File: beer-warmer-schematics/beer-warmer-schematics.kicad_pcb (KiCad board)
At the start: 4 copper layers, 60 x 42.8 mm, 33 parts, among them J1 USB_C_Receptacle_USB2.0_14P, J2 Screw_Terminal_01x02, J3 Conn_01x07_Socket, J4 Conn_01x07_Socket, J5 Conn_01x04_Pin, J6 Screw_Terminal_01x03, Q1 AOD4184A, U2 LM2596S-5, U3 CH224K

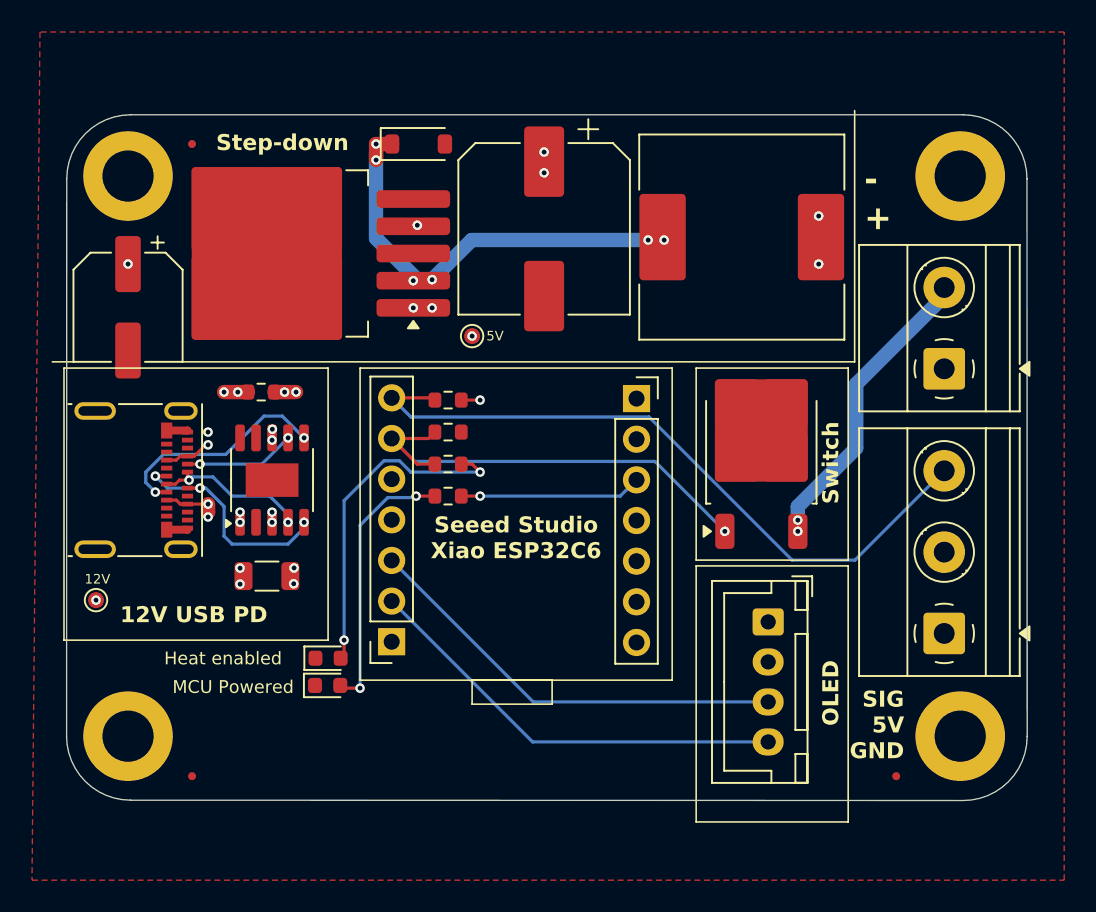
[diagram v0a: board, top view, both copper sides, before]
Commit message: fix a bunch of potential issues, add current sense
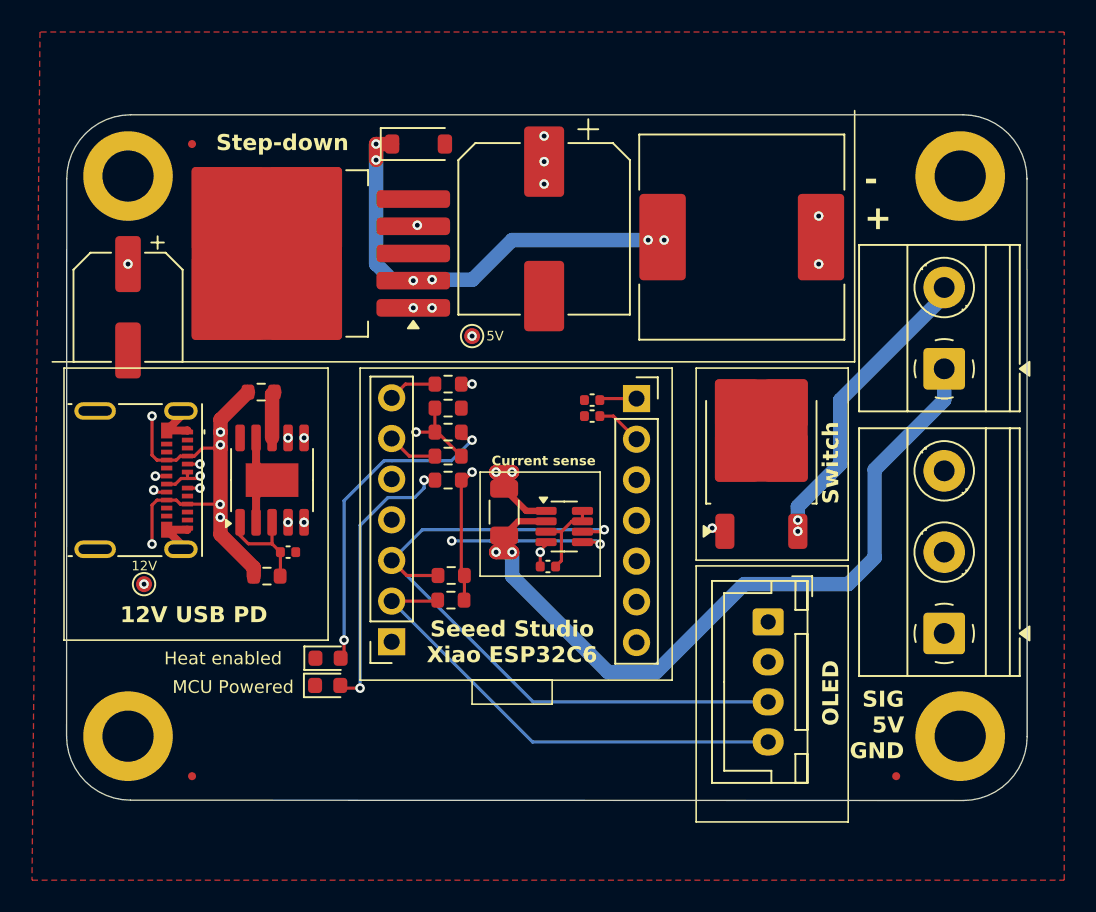
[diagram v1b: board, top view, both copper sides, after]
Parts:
- added C1: 1uF, Capacitor_SMD:C_0402_1005Metric, F.Cu at (152.5, 89.0)
- added C4: 1uF, Capacitor_SMD:C_0402_1005Metric, F.Cu at (152.5, 90.0)
- added C5: 1uF, Capacitor_SMD:C_0402_1005Metric, F.Cu at (149.7, 99.4)
- added C6: 1uF, Capacitor_SMD:C_0402_1005Metric, F.Cu at (133.5, 98.5)
- added R10: 2m, Resistor_SMD:R_1206_3216Metric, F.Cu at (147.0, 96.0)
- added R7: 200R, Resistor_SMD:R_0603_1608Metric, F.Cu at (143.5, 92.5)
- added R8: 4.7k, Resistor_SMD:R_0603_1608Metric, F.Cu at (143.7, 101.5)
- added R9: 4.7k, Resistor_SMD:R_0603_1608Metric, F.Cu at (143.7, 100.0)
- added U4: INA219AxDCN, Package_TO_SOT_SMD:SOT-23-8, F.Cu at (150.8, 96.9)
- R1: footprint Resistor_SMD:R_1206_3216Metric -> Resistor_SMD:R_0603_1608Metric
- moved TP1 3.16 mm to (124.5, 100.5)
- moved R3 2.00 mm to (143.5, 91.0)
- moved R2 1.50 mm to (143.5, 89.5)
- moved R4 1.00 mm to (143.5, 88.0)
- moved R6 1.00 mm to (143.5, 94.0)
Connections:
- net D3 renamed +3V3
- net Net-(J2-Pin_2) renamed HEAT-
- C2 pad 1: VDD -> VBUS
- J1 pad A4: Net-(J1-VBUS-PadA4) -> VBUS
- J1 pad A9: Net-(J1-VBUS-PadA4) -> VBUS
- J1 pad B4: Net-(J1-VBUS-PadA4) -> VBUS
- J1 pad B9: Net-(J1-VBUS-PadA4) -> VBUS
- J2 pad 1: VDD -> HEAT+
- J3 pad 2: GND -> Net-(J3-Pin_2)
- Q1 pad 1: D1 -> Net-(Q1-G)
- R1 pad 1: Net-(J1-VBUS-PadA4) -> VBUS
- R2 pad 1: D1 -> Net-(Q1-G)
- R3 pad 1: D1 -> Net-(Q1-G)
- R5 pad 1: Net-(J1-VBUS-PadA4) -> VBUS
- TP1 pad 1: VDD -> VBUS
- U2 pad 1: VDD -> VBUS
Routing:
- net HEAT+: track 0.00 -> 50.1 mm, vias 0 -> 2
- net VBUS: track 0.00 -> 33.4 mm, vias 0 -> 14
- net Net-(Q1-G): track 0.00 -> 26.9 mm, vias 0 -> 2
- net D1: track 29.4 -> 3.16 mm, vias 1 -> 0
- net Net-(J1-VBUS-PadA4): track 22.4 -> 0.00 mm, vias 8 -> 0
- net SDA: track 26.7 -> 45.5 mm, vias 0 -> 1
- net SCL: track 26.7 -> 45.4 mm, vias 0 -> 2
- net GND: track 2.78 -> 17.4 mm
- net +3V3: track 11.4 -> 20.8 mm
- net VDD: track 0.00 -> 6.62 mm, vias 11 -> 0
- net D0: track 43.8 -> 39.8 mm
- net +5V: track 1.18 -> 4.68 mm, vias 6 -> 7
- net Net-(J3-Pin_2): track 0.00 -> 2.89 mm
- net Net-(U3-VBUS): track 5.26 -> 2.92 mm, vias 4 -> 0
- net Net-(U3-DM): track 14.4 -> 12.5 mm
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- added copper zone on In2.Cu, net VBUS
- removed copper zone on In2.Cu, net VDD
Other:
- board text added: "Current sense"

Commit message: middle ground plane, 12v over dedicated tracks to avoid noise
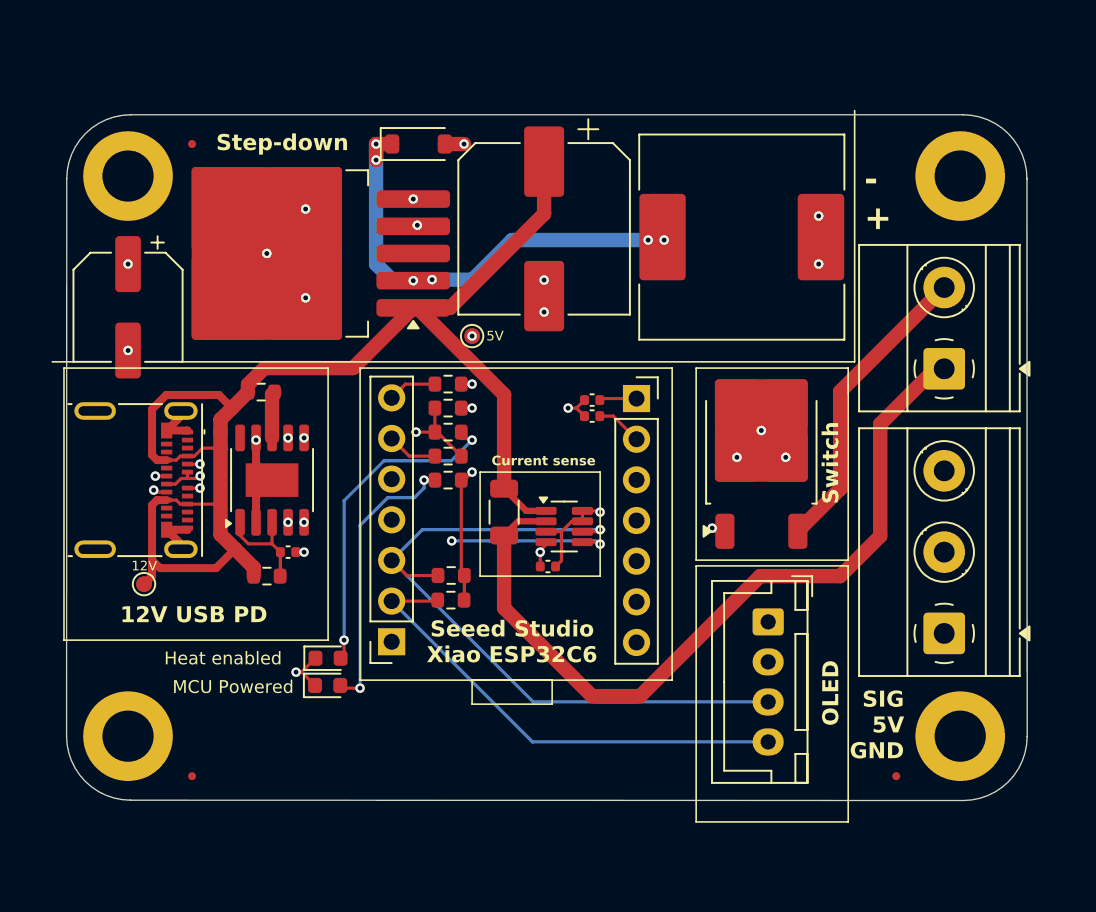
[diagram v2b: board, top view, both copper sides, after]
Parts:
- R10: value 2m -> 20m
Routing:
- net VBUS: track 33.4 -> 86.2 mm, vias 14 -> 0
- net GND: track 17.4 -> 26.0 mm, vias 0 -> 17
- net HEAT-: track 18.5 -> 19.0 mm, vias 2 -> 0
- net HEAT+: track 50.1 -> 49.9 mm, vias 2 -> 0
- added copper zone on In2.Cu, net GND
- removed copper zone on F.Cu, net GND
- removed copper zone on In2.Cu, net VBUS

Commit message: use a much simpler usb c component
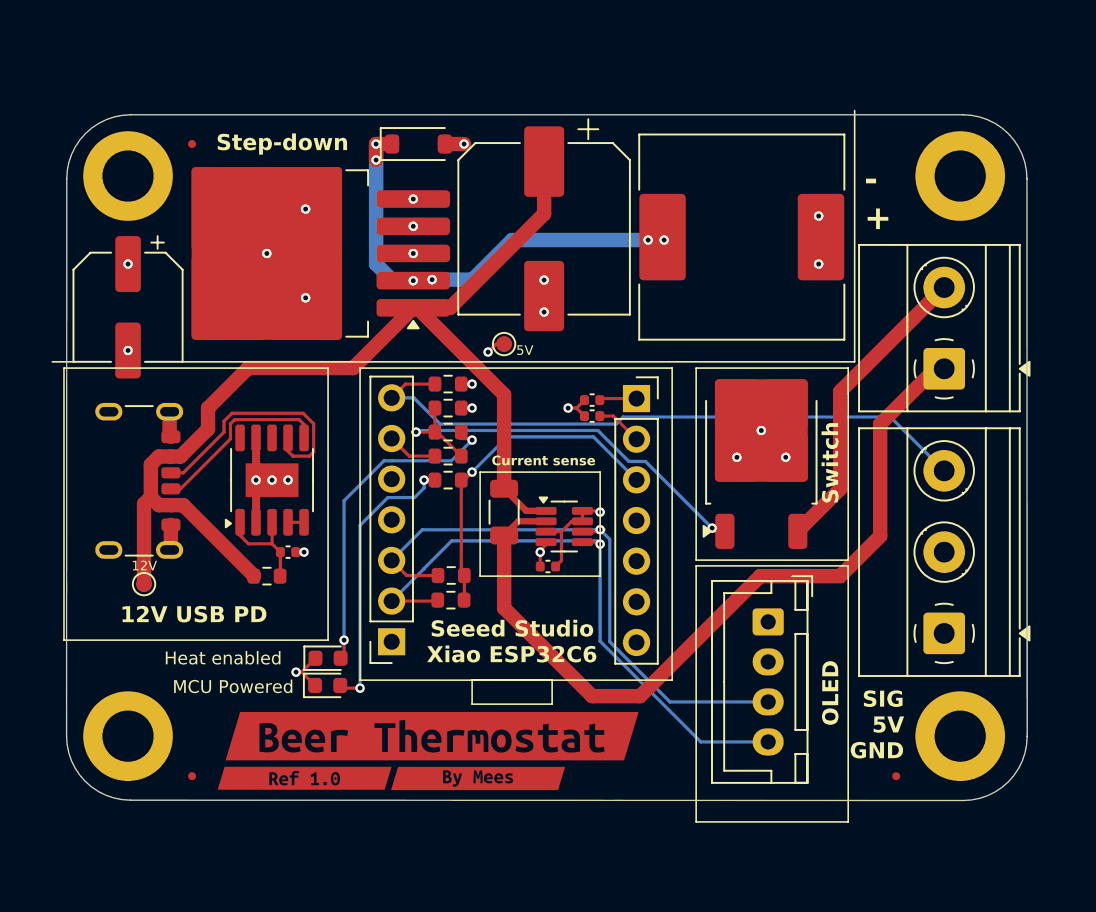
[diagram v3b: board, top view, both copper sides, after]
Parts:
- removed R5: 10K, Resistor_SMD:R_0603_1608Metric
- removed kibuzzard-67EA8950: G***, kibuzzard-67EA8950
- removed kibuzzard-67EA89B2: G***, kibuzzard-67EA89B2
- removed kibuzzard-67EA89F2: G***, kibuzzard-67EA89F2
- added kibuzzard-67EFB7C2: G***, kibuzzard-67EFB7C2, F.Cu at (142.5, 110.0)
- added kibuzzard-67EFB7CE: G***, kibuzzard-67EFB7CE, F.Cu at (134.5, 112.6)
- added kibuzzard-67EFB7D4: G***, kibuzzard-67EFB7D4, F.Cu at (145.4, 112.6)
- J1: footprint Library:USB_C_Receptacle_Molex_105450-0101 -> Connector_USB:USB_C_Receptacle_GCT_USB4125-xx-x_6P_TopMnt_Horizontal
- moved TP2 2.06 mm to (147.0, 85.5)
- moved J1 0.90 mm to (123.1, 94.0)
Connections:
- U3 pad 4: Net-(U3-DP) -> Net-(U3-DM)
- U3 pad 8: Net-(U3-VBUS) -> unconnected-(U3-VBUS-Pad8)
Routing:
- net VBUS: track 86.2 -> 68.8 mm
- net Net-(U3-DM): track 12.5 -> 1.00 mm, vias 3 -> 0
- net Net-(U3-DP): track 9.39 -> 0.00 mm, vias 2 -> 0
- net Net-(J1-CC1): track 6.96 -> 15.6 mm, vias 2 -> 0
- net SDA: track 45.5 -> 37.5 mm
- net SCL: track 45.4 -> 37.9 mm, vias 2 -> 1
- net Net-(U3-VBUS): track 2.92 -> 0.00 mm
- net GND: track 26.0 -> 23.4 mm, vias 17 -> 20
- net Net-(J1-CC2): track 13.6 -> 11.6 mm, vias 2 -> 0
- net +5V: track 4.68 -> 5.89 mm

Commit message: wider traces
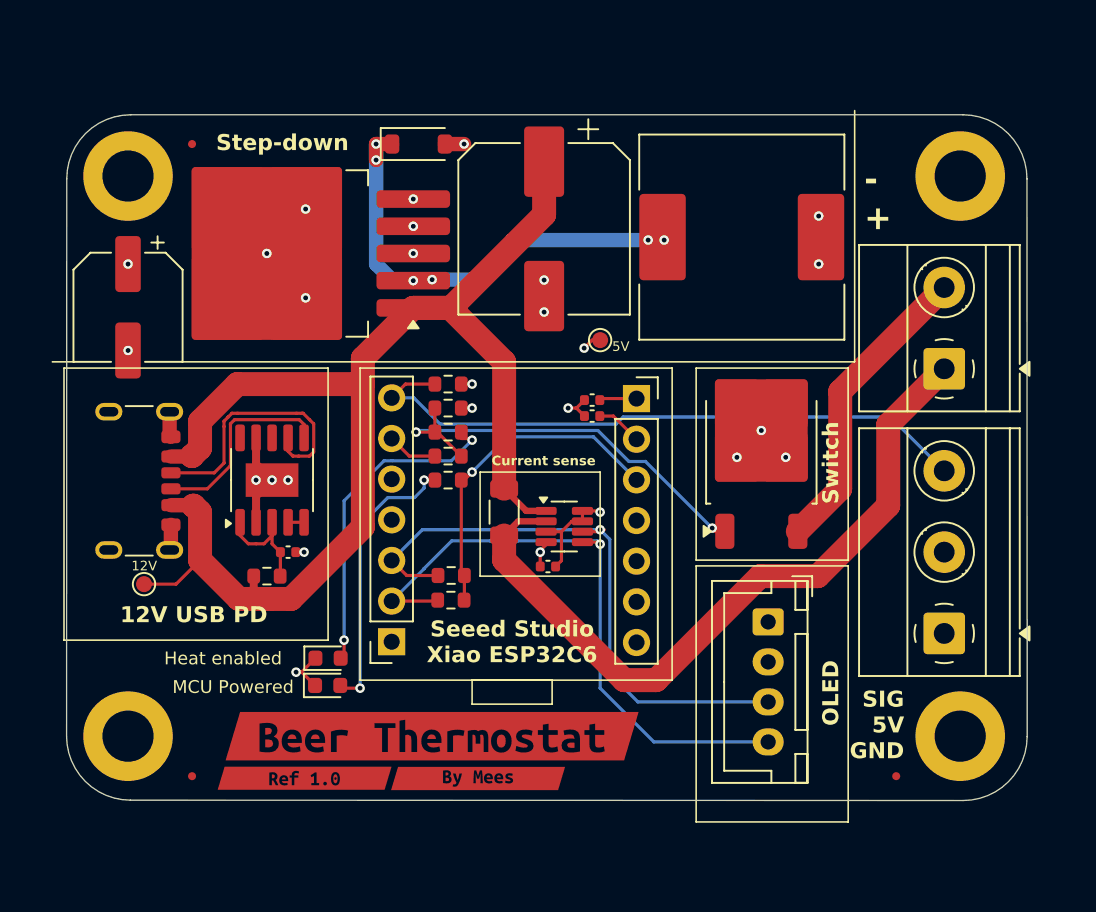
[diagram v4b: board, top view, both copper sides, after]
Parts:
- moved TP2 6.01 mm to (153.0, 85.3)
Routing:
- net VBUS: track 68.8 -> 86.1 mm
- net HEAT+: track 49.9 -> 46.2 mm
- net SCL: track 37.9 -> 39.7 mm
- net SDA: track 37.5 -> 38.7 mm
- net Net-(J1-CC1): track 15.6 -> 16.7 mm
- net VDD: track 6.62 -> 7.67 mm
- net Net-(J1-CC2): track 11.6 -> 12.6 mm

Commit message: clean up schematics, correct mosfet orientation
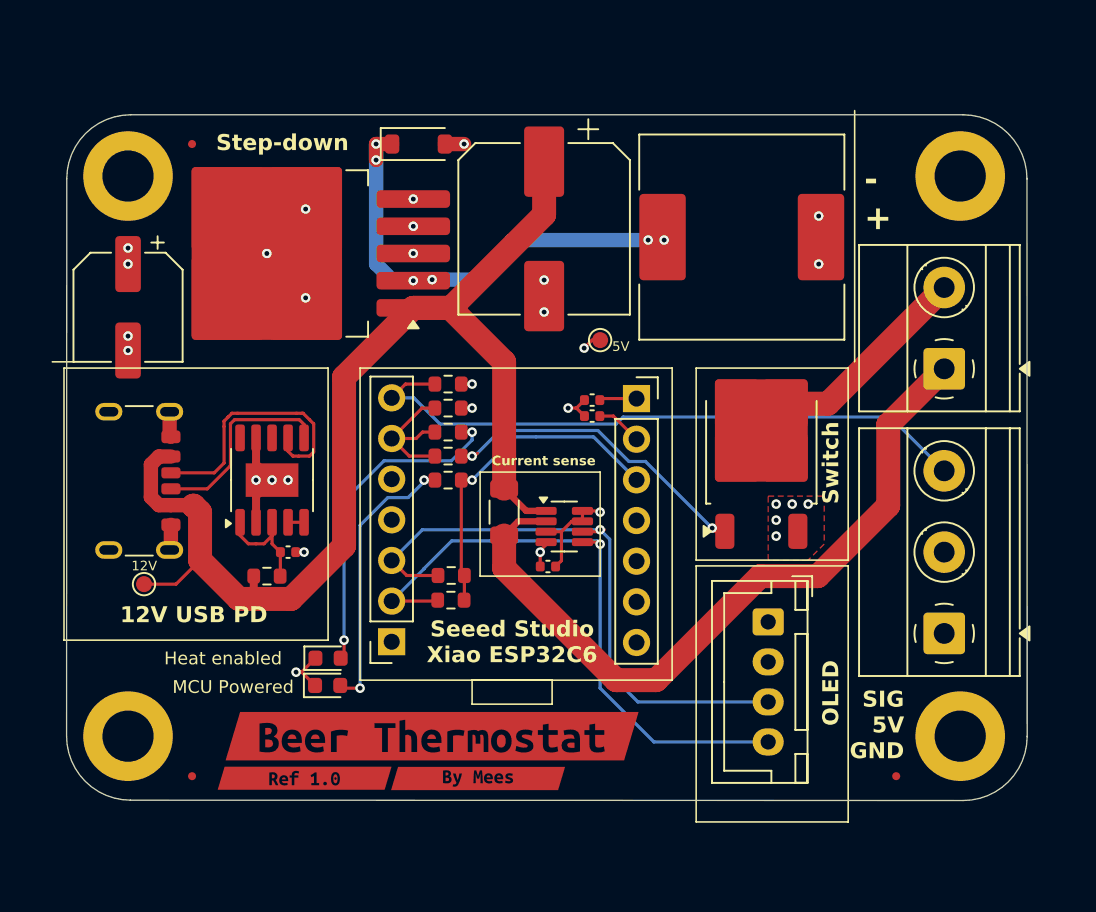
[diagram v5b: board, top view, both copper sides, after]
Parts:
- moved R8 1.54 mm to (143.7, 100.0), turned to 0 degrees
- moved R9 1.54 mm to (143.7, 101.5), turned to 0 degrees
- turned C1 to 180 degrees
- turned C5 to 180 degrees
- turned R7 to 0 degrees
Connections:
- C1 pad 1: GND -> +5V
- C1 pad 2: +5V -> GND
- C5 pad 1: +5V -> GND
- C5 pad 2: GND -> +5V
- Q1 pad 2: GND -> HEAT-
- Q1 pad 3: HEAT- -> GND
- R2 pad 1: Net-(Q1-G) -> D1
- R3 pad 1: Net-(Q1-G) -> D1
- R7 pad 1: Net-(Q1-G) -> D1
- R7 pad 2: D1 -> Net-(Q1-G)
- R8 pad 1: +3V3 -> SDA
- R8 pad 2: SCL -> +3V3
- R9 pad 1: +3V3 -> SCL
- R9 pad 2: SDA -> +3V3
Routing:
- net VBUS: track 86.1 -> 76.2 mm
- net D1: track 3.16 -> 9.66 mm
- net Net-(Q1-G): track 26.9 -> 20.4 mm
- net HEAT-: track 19.0 -> 12.9 mm
- net GND: vias 20 -> 23
- net +5V: vias 7 -> 8
- added copper zone on F.Cu, net GND

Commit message: led indicator on vbus power
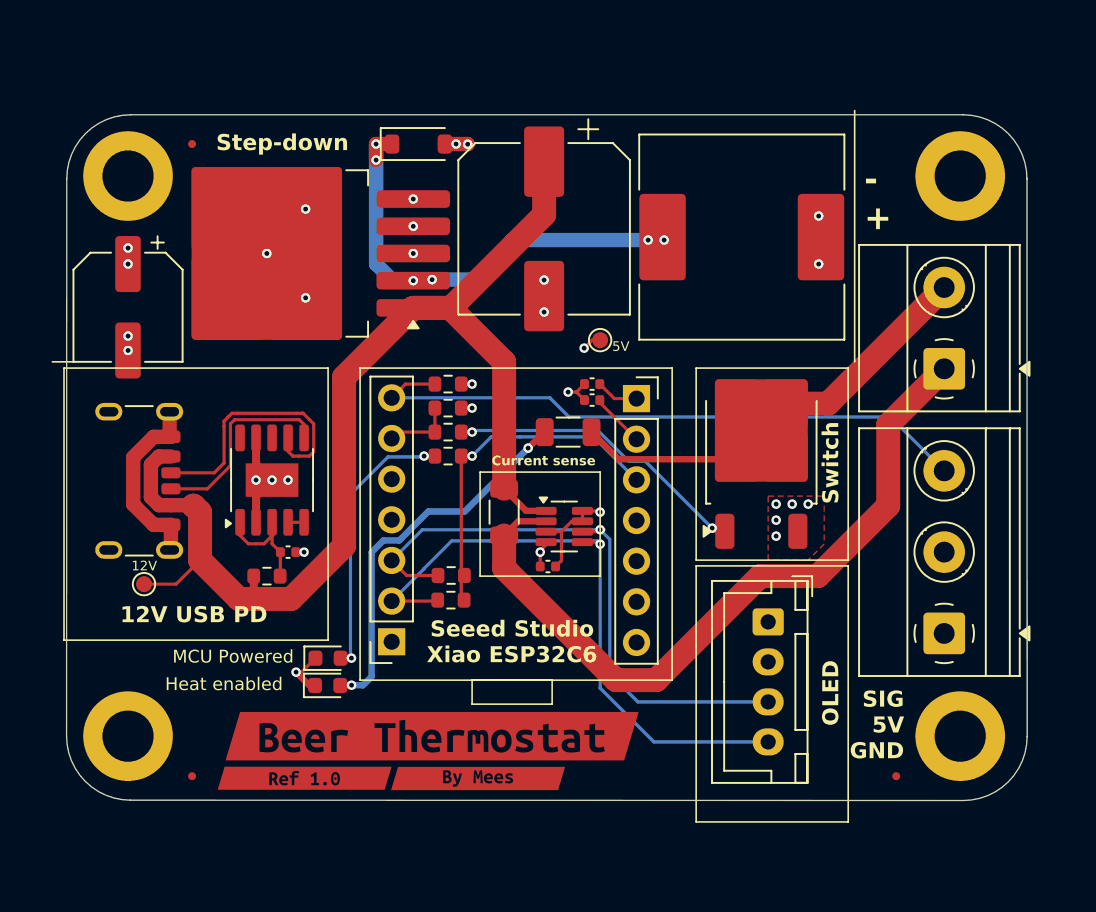
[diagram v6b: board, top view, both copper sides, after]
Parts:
- R3: value 200R -> 620R; footprint Resistor_SMD:R_0603_1608Metric -> Resistor_SMD:R_1206_3216Metric
- moved R3 7.50 mm to (151.0, 91.0), turned to 180 degrees
- moved D2 1.70 mm to (136.0, 106.8)
- moved D3 1.70 mm to (136.0, 105.1)
- moved R6 1.50 mm to (143.5, 92.5)
- moved R7 1.50 mm to (143.5, 91.0), turned to 180 degrees
- moved C1 1.00 mm to (152.5, 88.0)
- moved C4 1.00 mm to (152.5, 89.0)
- turned R2 to 180 degrees
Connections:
- R2 pad 1: D1 -> GND
- R2 pad 2: GND -> D1
- R3 pad 1: D1 -> HEAT-
- R7 pad 1: D1 -> Net-(Q1-G)
- R7 pad 2: Net-(Q1-G) -> D1
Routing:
- net HEAT-: track 12.9 -> 22.7 mm
- net GND: track 23.4 -> 32.3 mm, vias 23 -> 24
- net D1: track 9.66 -> 4.37 mm
- net Net-(D2-A): track 20.7 -> 23.9 mm
- net Net-(Q1-G): track 20.4 -> 19.2 mm
- net +3V3: track 20.8 -> 21.9 mm
- net Net-(J3-Pin_2): track 2.89 -> 3.40 mm
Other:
- board text added: "35mm"
- board text added: "52mm"

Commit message: remove some vias
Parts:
- moved TP2 0.41 mm to (152.9, 84.8)
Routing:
- net VBUS: track 76.2 -> 99.8 mm
- net GND: track 32.3 -> 35.2 mm, vias 24 -> 23
- net HEAT+: track 46.4 -> 47.6 mm
- net D1: track 4.37 -> 5.01 mm
- net Net-(D1-K): track 28.9 -> 28.8 mm, vias 6 -> 0
